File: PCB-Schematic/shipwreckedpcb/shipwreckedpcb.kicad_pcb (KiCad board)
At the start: 4 copper layers, 61.8 x 79.6 mm, 180 parts, among them J1 USB4105, J14 Conn_01x01, J15 Conn_01x01, J16 Conn_01x01, J17 Conn_01x01, J18 Conn_01x01, J19 Conn_01x01, J2 Waveshare 1.54" E-Ink, J20 Conn_01x01, J21 Conn_01x01, J22 Conn_01x01, J23 Conn_01x01, J24 Conn_01x01, J25 Conn_01x01, J26 Conn_01x01, J28 Conn_01x01, J29 Conn_01x01, J3 Conn_01x01, J30 Conn_01x01, J31 Conn_01x01, J32 Conn_01x01, J33 Conn_01x01, J34 Conn_01x01, J35 Conn_01x01, J36 Conn_01x01, J37 Conn_01x01, J38 Conn_01x01, J39 Conn_01x01, J4 Conn_01x01, J40 Conn_01x01, J5 SWD, J6 Conn_01x01, J7 Conn_01x01, Q1 Si1308EDL, SW1 BOOTSEL, SW10 Resistive, SW11 Clicky - THT, SW12 Clicky - SMD, SW13 Clicky - THT, SW14 Clicky - SMD, SW15 Clicky - THT, SW16 Clicky - SMD, SW17 Clicky - THT, SW18 Clicky - SMD, SW19 PWR Switch, SW2 RESET, SW3 Resistive, SW4 Resistive, SW5 Resistive, SW6 Resistive, SW7 Resistive, SW8 Resistive, SW9 Resistive, U1 RP2040, U2 W25Q128JVS, U3 Si4463, U4 TPS61200DRC, U5 AS179-92LF, U6 AMS1117-3.3, U7 PCA9555PW, Y1 ABM8-272-T3, Y2 X322530MOB4SI

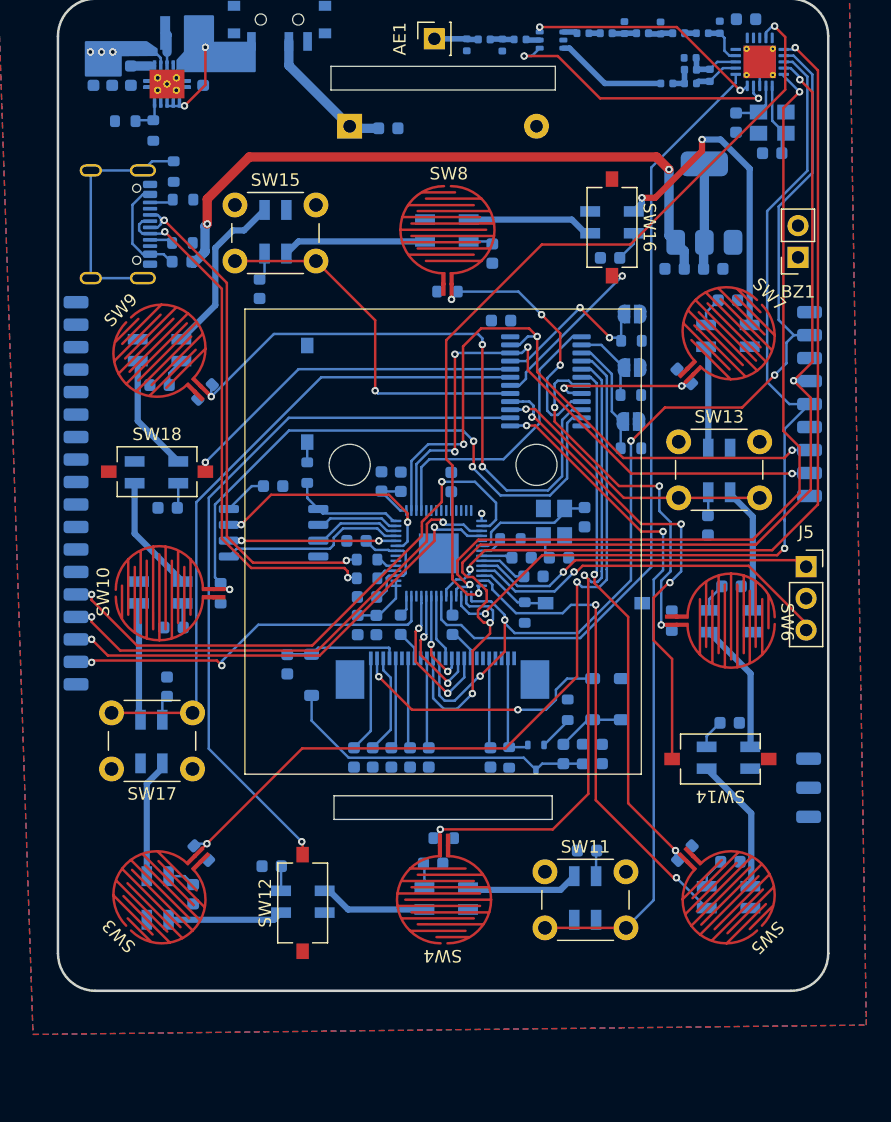
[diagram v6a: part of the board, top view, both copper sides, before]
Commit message: finished all the gpio + buzzer
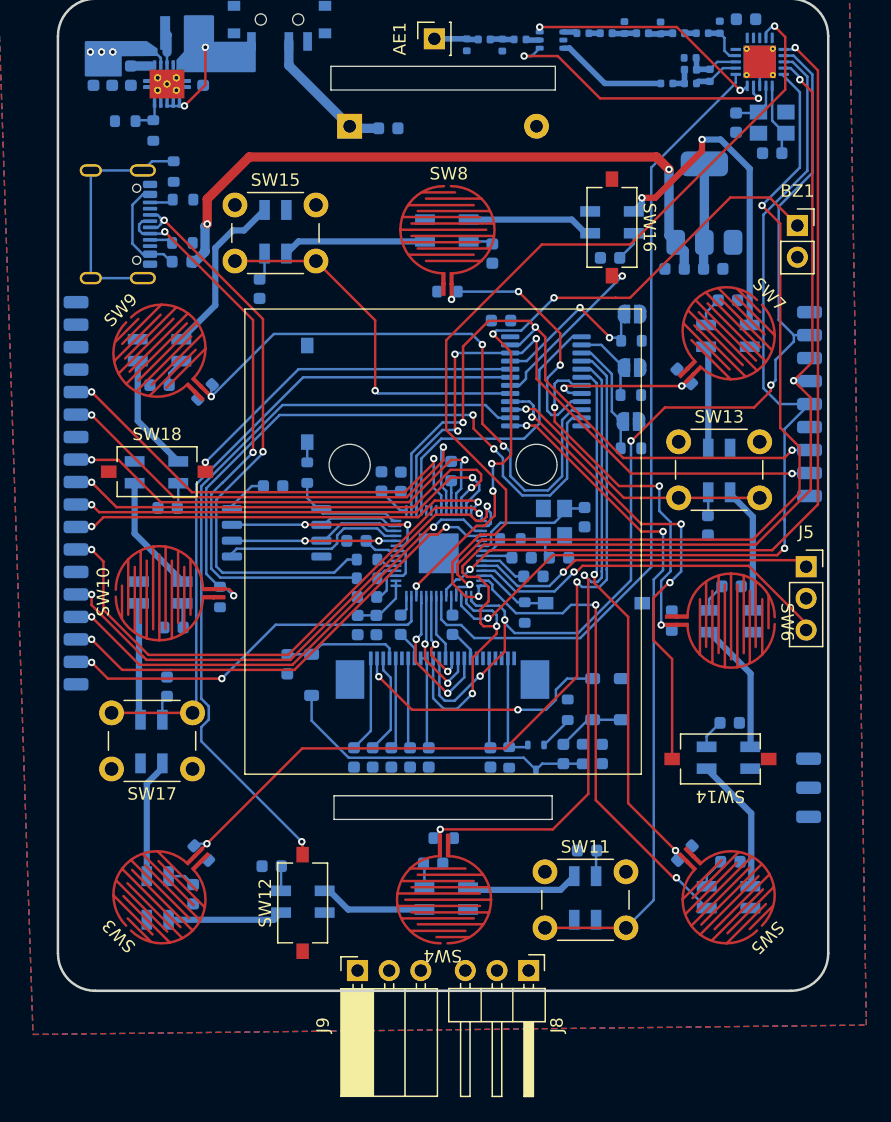
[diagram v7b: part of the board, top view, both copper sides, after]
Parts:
- added J8: B2B Male, Connector_PinHeader_2.54mm:PinHeader_1x03_P2.54mm_Horizontal, F.Cu at (153.9, 140.1)
- added J9: B2B Female, Connector_PinSocket_2.54mm:PinSocket_1x03_P2.54mm_Horizontal, F.Cu at (140.2, 140.1)
- moved BZ1 2.55 mm to (175.5, 80.3), turned to 0 degrees
- moved C6 0.88 mm to (147.7, 100.0)
- moved R17 0.30 mm to (129.2, 110.2)
- moved U2 0.25 mm to (133.7, 105.0)
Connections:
- J6 pad 1: /GPIO4 -> +3V3
- J7 pad 1: /GPIO5 -> +3V3
- U1 pad 5: /GPIO3 -> /B2B_DCT
- U1 pad 6: /GPIO4 -> /B2B_TX
- U1 pad 7: /GPIO5 -> /B2B_RX
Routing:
- net /GPIO28_ADC2_BUZZER: track 0.00 -> 55.8 mm, vias 0 -> 5
- net /GPIO12: track 0.60 -> 43.9 mm, vias 1 -> 2
- net /GPIO7: track 0.00 -> 39.8 mm, vias 0 -> 2
- net /GPIO9: track 0.00 -> 38.4 mm, vias 0 -> 2
- net /GPIO8: track 0.00 -> 38.4 mm, vias 0 -> 2
- net /GPIO6: track 0.00 -> 37.8 mm, vias 0 -> 2
- net /GPIO10: track 0.00 -> 36.5 mm, vias 0 -> 2
- net /GPIO11: track 0.00 -> 34.1 mm, vias 0 -> 2
- net /USB_DP: track 41.6 -> 47.3 mm
- net /SI_IO1: track 65.1 -> 70.1 mm
- net /USB_DM: track 42.6 -> 47.0 mm
- net /BUTT_8: track 49.3 -> 53.6 mm
- net /QSPI_SD3: track 19.3 -> 16.5 mm
- net /BUTT_10: track 58.6 -> 61.3 mm
- net /GPIO13: track 46.1 -> 44.0 mm
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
